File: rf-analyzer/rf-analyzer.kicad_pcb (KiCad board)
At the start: 4 copper layers, 101.6 x 53.3 mm, 57 parts, among them J1 Conn_Coaxial, J2 RF_Shield_Two_Pieces, J3 Conn_Coaxial, U1 AD8302, U2 AD8302, U3 TLV3501_DBV, U4 HMC363S8G, U5 OPA695, U6 LTC2309_TSSOP

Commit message: Populated and routed PCB board.
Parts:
- removed D1, D2, D3, D4: 1N5711, Diode_SMD:D_SOD-323
- removed R11, R12: 100kΩ, Capacitor_SMD:C_0402_1005Metric
- added C28: 1nF, Capacitor_SMD:C_0402_1005Metric, F.Cu at (122.7, 114.9)
- added C29: 1nF, Capacitor_SMD:C_0402_1005Metric, F.Cu at (116.8, 120.7)
- added C30: 1nF, Capacitor_SMD:C_0402_1005Metric, B.Cu at (124.5, 116.8)
- added C31: 100nF, Capacitor_SMD:C_0402_1005Metric, B.Cu at (124.5, 119.4)
- added C32: 100nF, Capacitor_SMD:C_0402_1005Metric, F.Cu at (127.6, 120.7)
- added U7: AD8362, Package_SO:TSSOP-16_4.4x5mm_P0.65mm, F.Cu at (122.3, 118.3)
- C11: value 1nF -> 10nF
- C23: value 100nF -> 10nF
- C25: value 100nF -> 1nF
- R2: value 33Ω -> 66.5Ω
- R5: value 22Ω -> 44.2Ω
- moved C21 33.1 mm to (169.5, 86.4), turned to 180 degrees
- moved R16 32.7 mm to (170.8, 86.5), turned to 90 degrees
- moved U6 30.1 mm to (166.4, 88.9), turned to 180 degrees
- moved C27 30.0 mm to (163.8, 91.0), turned to 270 degrees
- moved C26 28.4 mm to (165.9, 90.2), turned to 0 degrees
- moved C22 25.7 mm to (166.4, 91.4), turned to 0 degrees
- moved R4 25.3 mm to (139.2, 116.2), turned to 180 degrees
- moved R15 24.7 mm to (170.8, 90.0), turned to 270 degrees
- moved C14 23.7 mm to (138.4, 113.7)
- moved C13 23.6 mm to (141.6, 116.2)
- moved U3 23.4 mm to (139.1, 113.5), turned to 90 degrees
- moved C25 22.7 mm to (120.2, 114.9), turned to 180 degrees
- moved C15 20.5 mm to (139.1, 109.9), turned to 270 degrees
- moved R8 18.6 mm to (139.7, 99.5), turned to 270 degrees
- moved R7 16.8 mm to (141.0, 99.5), turned to 270 degrees
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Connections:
- C23 pad 1: GNDA -> Net-(C23-Pad1)
- C23 pad 2: fwd_pwr -> GNDA
- C25 pad 1: GNDA -> Net-(C25-Pad1)
- C25 pad 2: refl_pwr -> GNDA
- C6 pad 2: GND -> GNDA
- C7 pad 2: GND -> GNDA
- U1 pad 14: Net-(U1-Pad14) -> (no net)
- U1 pad 8: Net-(U1-Pad8) -> (no net)
- U2 pad 14: Net-(U2-Pad14) -> (no net)
- U2 pad 8: Net-(U2-Pad8) -> (no net)
- U4 pad 1: Net-(U4-Pad1) -> (no net)
- U6 pad 11: shft_mag -> mag
- U6 pad 12: shft_vref -> vref
- U6 pad 13: shft_phase -> phase
- U6 pad 14: fwd_pwr -> shft_mag
- U6 pad 15: mag -> shft_vref
- U6 pad 16: vref -> shft_phase
- U6 pad 17: phase -> fwd_pwr
- U6 pad 18: refl_pwr -> GNDA
- U6 pad 4: Net-(U6-Pad4) -> (no net)
- U6 pad 5: Net-(U6-Pad5) -> (no net)
- XA1 pad 5V2: Net-(XA1-Pad5V2) -> (no net)
- XA1 pad A0: Net-(XA1-PadA0) -> (no net)
- XA1 pad A1: Net-(XA1-PadA1) -> (no net)
- XA1 pad A10: Net-(XA1-PadA10) -> (no net)
- XA1 pad A11: Net-(XA1-PadA11) -> (no net)
- XA1 pad A2: Net-(XA1-PadA2) -> (no net)
- XA1 pad A3: Net-(XA1-PadA3) -> (no net)
- XA1 pad A4: Net-(XA1-PadA4) -> (no net)
- XA1 pad A5: Net-(XA1-PadA5) -> (no net)
- XA1 pad A6: Net-(XA1-PadA6) -> (no net)
- XA1 pad A7: Net-(XA1-PadA7) -> (no net)
- XA1 pad A8: Net-(XA1-PadA8) -> (no net)
- XA1 pad A9: Net-(XA1-PadA9) -> (no net)
- XA1 pad AREF: Net-(XA1-PadAREF) -> (no net)
- XA1 pad CANR: Net-(XA1-PadCANR) -> (no net)
- XA1 pad CANT: Net-(XA1-PadCANT) -> (no net)
- XA1 pad D0: Net-(XA1-PadD0) -> (no net)
- XA1 pad D1: Net-(XA1-PadD1) -> (no net)
- XA1 pad D10: Net-(XA1-PadD10) -> (no net)
- XA1 pad D11: Net-(XA1-PadD11) -> (no net)
- XA1 pad D12: Net-(XA1-PadD12) -> (no net)
- XA1 pad D13: Net-(XA1-PadD13) -> (no net)
- XA1 pad D14: Net-(XA1-PadD14) -> (no net)
- XA1 pad D15: Net-(XA1-PadD15) -> (no net)
- XA1 pad D16: Net-(XA1-PadD16) -> (no net)
- XA1 pad D17: Net-(XA1-PadD17) -> (no net)
- XA1 pad D18: Net-(XA1-PadD18) -> (no net)
- XA1 pad D19: Net-(XA1-PadD19) -> (no net)
- XA1 pad D2: Net-(XA1-PadD2) -> (no net)
- XA1 pad D20: Net-(XA1-PadD20) -> (no net)
- XA1 pad D21: Net-(XA1-PadD21) -> (no net)
- XA1 pad D23: Net-(XA1-PadD23) -> (no net)
- XA1 pad D24: Net-(XA1-PadD24) -> (no net)
- XA1 pad D25: Net-(XA1-PadD25) -> (no net)
- XA1 pad D26: Net-(XA1-PadD26) -> (no net)
- XA1 pad D27: Net-(XA1-PadD27) -> (no net)
- XA1 pad D28: Net-(XA1-PadD28) -> (no net)
- XA1 pad D29: Net-(XA1-PadD29) -> (no net)
- XA1 pad D3: Net-(XA1-PadD3) -> (no net)
- XA1 pad D30: Net-(XA1-PadD30) -> (no net)
- XA1 pad D31: Net-(XA1-PadD31) -> (no net)
- XA1 pad D32: Net-(XA1-PadD32) -> (no net)
- XA1 pad D33: Net-(XA1-PadD33) -> (no net)
- XA1 pad D34: Net-(XA1-PadD34) -> (no net)
- XA1 pad D35: Net-(XA1-PadD35) -> (no net)
- XA1 pad D36: Net-(XA1-PadD36) -> (no net)
- XA1 pad D37: Net-(XA1-PadD37) -> (no net)
- XA1 pad D38: Net-(XA1-PadD38) -> (no net)
- XA1 pad D39: Net-(XA1-PadD39) -> (no net)
- XA1 pad D4: Net-(XA1-PadD4) -> (no net)
- XA1 pad D40: Net-(XA1-PadD40) -> (no net)
- XA1 pad D41: Net-(XA1-PadD41) -> (no net)
- XA1 pad D42: Net-(XA1-PadD42) -> (no net)
- XA1 pad D43: Net-(XA1-PadD43) -> (no net)
- XA1 pad D44: Net-(XA1-PadD44) -> (no net)
- XA1 pad D45: Net-(XA1-PadD45) -> (no net)
- XA1 pad D46: Net-(XA1-PadD46) -> (no net)
- XA1 pad D47: Net-(XA1-PadD47) -> (no net)
- XA1 pad D48: Net-(XA1-PadD48) -> (no net)
- XA1 pad D49: Net-(XA1-PadD49) -> (no net)
- XA1 pad D5: Net-(XA1-PadD5) -> (no net)
- XA1 pad D50: Net-(XA1-PadD50) -> (no net)
- XA1 pad D51: Net-(XA1-PadD51) -> (no net)
- XA1 pad D52: Net-(XA1-PadD52) -> (no net)
- XA1 pad D53: Net-(XA1-PadD53) -> (no net)
- XA1 pad D6: Net-(XA1-PadD6) -> (no net)
- XA1 pad D7: Net-(XA1-PadD7) -> (no net)
- XA1 pad D8: Net-(XA1-PadD8) -> (no net)
- XA1 pad D9: Net-(XA1-PadD9) -> (no net)
- XA1 pad DAC0: Net-(XA1-PadDAC0) -> (no net)
- XA1 pad DAC1: Net-(XA1-PadDAC1) -> (no net)
- XA1 pad GND4: Net-(XA1-PadGND4) -> (no net)
- XA1 pad IORF: Net-(XA1-PadIORF) -> (no net)
- XA1 pad MISO: Net-(XA1-PadMISO) -> (no net)
- XA1 pad MOSI: Net-(XA1-PadMOSI) -> (no net)
- XA1 pad RST1: Net-(XA1-PadRST1) -> (no net)
- XA1 pad RST2: Net-(XA1-PadRST2) -> (no net)
- XA1 pad SCK: Net-(XA1-PadSCK) -> (no net)
- XA1 pad VIN: Net-(XA1-PadVIN) -> (no net)
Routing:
- net +5V: track 13.0 -> 183.8 mm, vias 3 -> 10
- net +3V3: track 0.00 -> 72.7 mm, vias 0 -> 2
- net SCL: track 0.00 -> 66.3 mm, vias 0 -> 1
- net SDA: track 0.00 -> 61.6 mm, vias 0 -> 1
- net freq_count: track 0.00 -> 60.9 mm, vias 0 -> 1
- net fwd_pwr: track 1.74 -> 58.6 mm, vias 0 -> 2
- net mag: track 0.00 -> 47.9 mm, vias 0 -> 2
- net phase: track 0.00 -> 47.9 mm, vias 0 -> 2
- net vref: track 0.00 -> 46.9 mm, vias 0 -> 2
- net shft_phase: track 0.00 -> 46.1 mm, vias 0 -> 2
- net shft_mag: track 0.00 -> 45.9 mm, vias 0 -> 2
- net shft_vref: track 0.00 -> 44.4 mm, vias 0 -> 2
- net fwd_sig_dc: track 4.44 -> 30.7 mm, vias 0 -> 2
- net Net-(D1-Pad1): track 5.79 -> 0.00 mm
- net fwd_sig: track 21.9 -> 26.3 mm
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
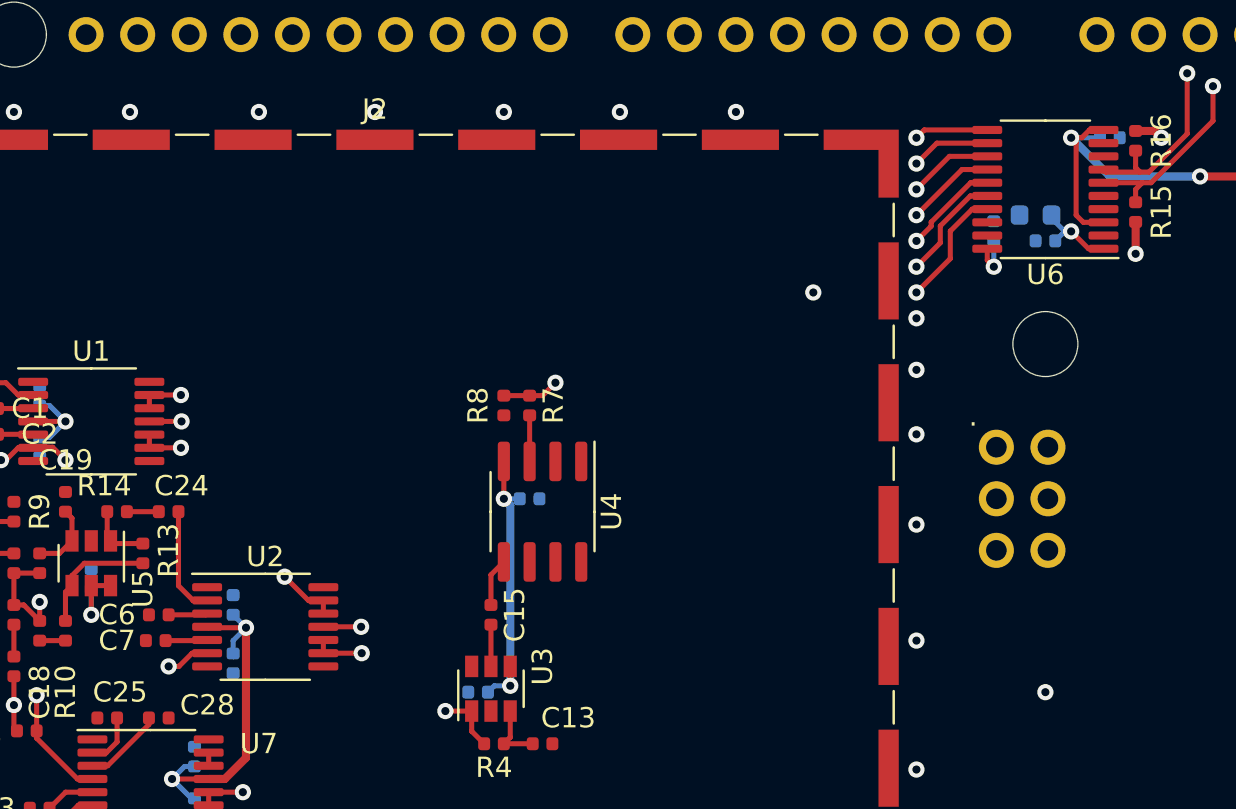
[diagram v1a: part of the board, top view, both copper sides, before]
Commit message: Added some vias to ensure all layers are filled with a ground plane.
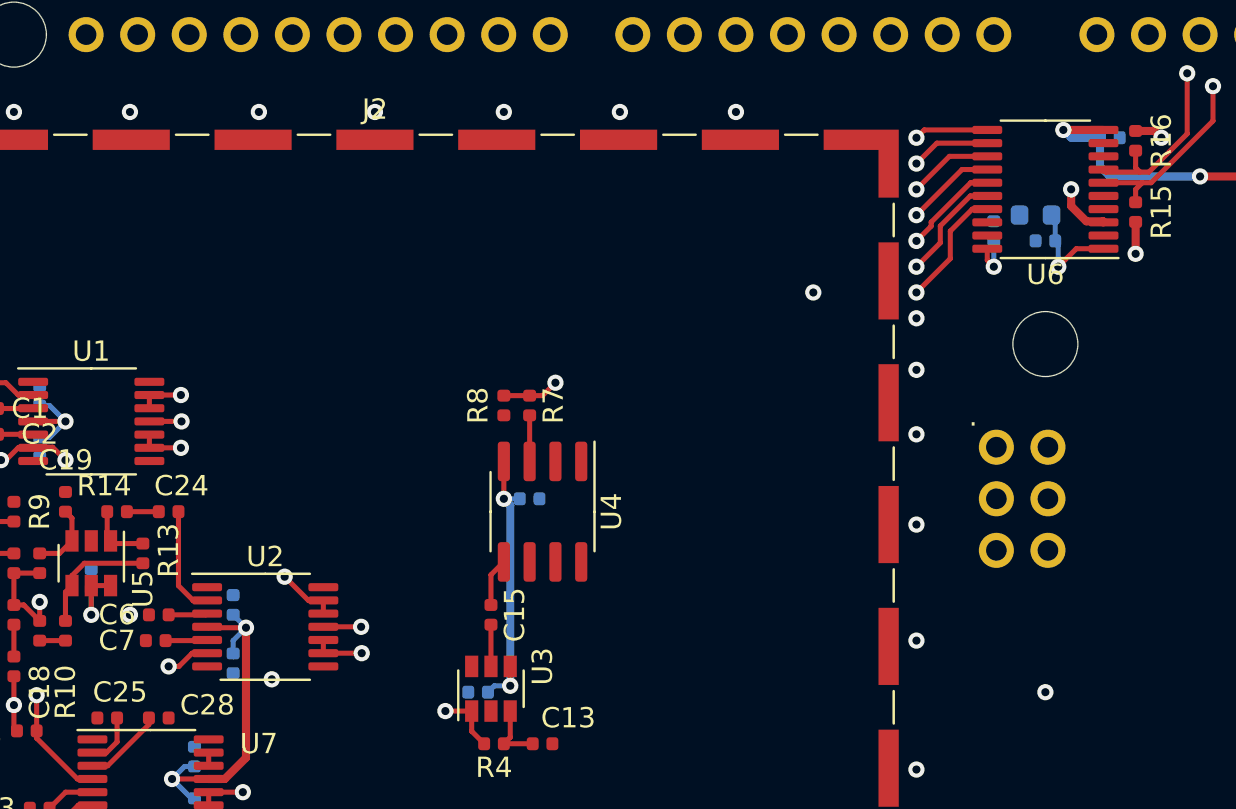
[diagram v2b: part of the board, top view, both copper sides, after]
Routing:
- net Net-(C22-Pad2): track 4.00 -> 5.42 mm
- net +5V: vias 10 -> 11
- net GNDA: vias 42 -> 44
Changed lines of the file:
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@@
     (thickness 1.6)
     (drawings 9)
-    (tracks 406)
+    (tracks 416)
     (zones 0)
     (modules 57)
@@
   (page A4)
   (layers
-    (0 F.Cu signal)
+    (0 F.Cu signal hide)
     (1 F2.Cu signal hide)
-    (2 B2.Cu signal hide)
+    (2 B2.Cu signal)
     (31 B.Cu signal hide)
     (32 B.Adhes user hide)
@@
   )
   (setup
-    (last_trace_width 0.25)
+    (last_trace_width 0.4)
     (user_trace_width 0.4)
     (trace_clearance 0.2)
@@
   (via (at 181.61 122.555) (size 0.8) (drill 0.4) (layers F.Cu B.Cu) (net 1))
   (via (at 166.37 113.665) (size 0.8) (drill 0.4) (layers F.Cu B.Cu) (net 1))
+  (via (at 121.285 109.855) (size 0.8) (drill 0.4) (layers F.Cu B.Cu) (net 1))
+  (via (at 128.27 113.03) (size 0.8) (drill 0.4) (layers F.Cu B.Cu) (net 1))
   (segment (start 116.5025 99.695) (end 116.5175 99.68) (width 0.25) (layer F.Cu) (net 2))
   (segment (start 114.785 99.695) (end 116.5025 99.695) (width 0.25) (layer F.Cu) (net 2))
@@
   (via (at 139.7 104.14) (size 0.8) (drill 0.4) (layers F.Cu B.Cu) (net 4))
   (segment (start 140.485 104.14) (end 139.7 104.14) (width 0.25) (layer B.Cu) (net 4))
-  (segment (start 169.2325 85.975) (end 168.543942 85.975) (width 0.25) (layer F.Cu) (net 4))
-  (segment (start 168.543942 85.975) (end 168.158942 86.36) (width 0.25) (layer F.Cu) (net 4))
-  (segment (start 168.158942 86.36) (end 167.64 86.36) (width 0.25) (layer F.Cu) (net 4))
-  (segment (start 167.64 86.36) (end 167.64 86.36) (width 0.25) (layer F.Cu) (net 4))
-  (via (at 167.64 86.36) (size 0.8) (drill 0.4) (layers F.Cu B.Cu) (net 4))
-  (segment (start 169.06 86.36) (end 167.64 86.36) (width 0.25) (layer B.Cu) (net 4))
-  (segment (start 168.240011 90.525) (end 167.885011 90.17) (width 0.25) (layer F.Cu) (net 4))
-  (segment (start 169.2325 90.525) (end 168.240011 90.525) (width 0.25) (layer F.Cu) (net 4))
-  (segment (start 167.885011 86.605011) (end 167.64 86.36) (width 0.25) (layer F.Cu) (net 4))
-  (segment (start 167.885011 90.17) (end 167.885011 86.605011) (width 0.25) (layer F.Cu) (net 4))
   (segment (start 117.309999 101.130001) (end 117.309999 106.514999) (width 0.4) (layer B2.Cu) (net 4))
   (segment (start 118.11 100.33) (end 117.309999 101.130001) (width 0.4) (layer B2.Cu) (net 4))
@@
   (segment (start 125.957124 117.94) (end 127 116.897124) (width 0.4) (layer F.Cu) (net 4))
   (segment (start 125.1625 117.94) (end 125.957124 117.94) (width 0.4) (layer F.Cu) (net 4))
-  (segment (start 167.64 86.36) (end 169.545 88.265) (width 0.4) (layer B.Cu) (net 4))
   (segment (start 169.545 88.265) (end 173.99 88.265) (width 0.4) (layer B.Cu) (net 4))
   (segment (start 173.99 88.265) (end 173.99 88.265) (width 0.4) (layer B.Cu) (net 4))
@@
   (segment (start 192.405 83.185) (end 194.31 81.28) (width 0.4) (layer F.Cu) (net 4))
   (segment (start 194.31 81.28) (end 196.85 81.28) (width 0.4) (layer F.Cu) (net 4))
-  (segment (start 165.735 88.265) (end 167.64 86.36) (width 0.4) (layer B2.Cu) (net 4))
   (segment (start 165.735 93.345) (end 165.735 88.265) (width 0.4) (layer B2.Cu) (net 4))
   (segment (start 145.73 113.35) (end 140.015 113.35) (width 0.4) (layer B2.Cu) (net 4))
@@
   (segment (start 140.015 104.455) (end 139.7 104.14) (width 0.4) (layer B.Cu) (net 4))
   (segment (start 140.015 113.35) (end 140.015 104.455) (width 0.4) (layer B.Cu) (net 4))
+  (segment (start 169.2325 85.975) (end 167.255 85.975) (width 0.4) (layer F.Cu) (net 4))
+  (segment (start 169.2325 90.525) (end 169.19 90.525) (width 0.4) (layer F.Cu) (net 4))
+  (segment (start 167.255 85.975) (end 167.255 85.975) (width 0.4) (layer F.Cu) (net 4))
+  (via (at 167.255 85.975) (size 0.8) (drill 0.4) (layers F.Cu B.Cu) (net 4))
+  (segment (start 168.387886 90.47501) (end 167.64 89.727124) (width 0.4) (layer F.Cu) (net 4))
+  (segment (start 169.21501 90.47501) (end 168.387886 90.47501) (width 0.4) (layer F.Cu) (net 4))
+  (segment (start 169.2325 90.4925) (end 169.21501 90.47501) (width 0.4) (layer F.Cu) (net 4))
+  (segment (start 169.2325 90.525) (end 169.2325 90.4925) (width 0.4) (layer F.Cu) (net 4))
+  (segment (start 167.64 89.727124) (end 167.64 88.9) (width 0.4) (layer F.Cu) (net 4))
+  (segment (start 167.64 88.9) (end 167.64 88.9) (width 0.4) (layer F.Cu) (net 4))
+  (via (at 167.64 88.9) (size 0.8) (drill 0.4) (layers F.Cu B.Cu) (net 4))
+  (segment (start 167.005 88.265) (end 167.64 88.9) (width 0.4) (layer B2.Cu) (net 4))
+  (segment (start 165.735 88.265) (end 167.005 88.265) (width 0.4) (layer B2.Cu) (net 4))
+  (segment (start 165.735 87.495) (end 167.255 85.975) (width 0.4) (layer B2.Cu) (net 4))
+  (segment (start 165.735 88.265) (end 165.735 87.495) (width 0.4) (layer B2.Cu) (net 4))
+  (segment (start 169.06 87.78) (end 169.06 86.36) (width 0.4) (layer B.Cu) (net 4))
+  (segment (start 169.545 88.265) (end 169.06 87.78) (width 0.4) (layer B.Cu) (net 4))
+  (segment (start 167.64 86.36) (end 167.255 85.975) (width 0.4) (layer B.Cu) (net 4))
+  (segment (start 169.06 86.36) (end 167.64 86.36) (width 0.4) (layer B.Cu) (net 4))
   (segment (start 125.025 109.855) (end 125.085 109.795) (width 0.25) (layer F.Cu) (net 5))
   (segment (start 123.19 109.855) (end 125.025 109.855) (width 0.25) (layer F.Cu) (net 5))
@@
   (segment (start 118.43 105.095) (end 118.11 104.775) (width 0.25) (layer F.Cu) (net 18))
   (segment (start 118.43 106.215) (end 118.43 105.095) (width 0.25) (layer F.Cu) (net 18))
-  (segment (start 168.495 91.825) (end 167.64 90.97) (width 0.25) (layer F.Cu) (net 19))
-  (segment (start 169.2325 91.825) (end 168.495 91.825) (width 0.25) (layer F.Cu) (net 19))
-  (segment (start 167.64 90.97) (end 167.64 90.97) (width 0.25) (layer F.Cu) (net 19))
-  (via (at 167.64 90.97) (size 0.8) (drill 0.4) (layers F.Cu B.Cu) (net 19))
-  (segment (start 167.325 90.97) (end 166.855 91.44) (width 0.25) (layer B.Cu) (net 19))
-  (segment (start 167.64 90.97) (end 167.325 90.97) (width 0.25) (layer B.Cu) (net 19))
-  (segment (start 166.675 90.32) (end 167.325 90.97) (width 0.25) (layer B.Cu) (net 19))
   (segment (start 166.675 90.17) (end 166.675 90.32) (width 0.25) (layer B.Cu) (net 19))
+  (segment (start 169.2325 91.825) (end 167.89 91.825) (width 0.25) (layer F.Cu) (net 19))
+  (segment (start 167.89 91.825) (end 167.005 92.71) (width 0.25) (layer F.Cu) (net 19))
+  (segment (start 167.005 92.71) (end 167.005 92.71) (width 0.25) (layer F.Cu) (net 19))
+  (via (at 167.005 92.71) (size 0.8) (drill 0.4) (layers F.Cu B.Cu) (net 19))
+  (segment (start 167.005 91.59) (end 166.855 91.44) (width 0.25) (layer B.Cu) (net 19))
+  (segment (start 167.005 92.71) (end 167.005 91.59) (width 0.25) (layer B.Cu) (net 19))
+  (segment (start 166.855 90.35) (end 166.675 90.17) (width 0.25) (layer B.Cu) (net 19))
+  (segment (start 166.855 91.44) (end 166.855 90.35) (width 0.25) (layer B.Cu) (net 19))
   (segment (start 125.1625 119.24) (end 125.1625 118.59) (width 0.25) (layer F.Cu) (net 20))
   (segment (start 125.1625 118.59) (end 126.845 118.59) (width 0.25) (layer F.Cu) (net 20))
